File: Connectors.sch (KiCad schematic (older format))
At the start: 11 parts, among them J201 Conn_01x10, J202 Conn_ARM_JTAG_SWD_10, J203 Conn_02x03_Counter_Clockwise, J204 USB_B_Micro, J205 Conn_01x04

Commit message: completed layout
Signed-off-by: Thomas Schmid <tom@binary-kitchen.de>
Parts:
- added U201: USBLC6-2SC6, Package_TO_SOT_SMD:SOT-666, symbol Power_Protection:USBLC6-2SC6
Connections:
- net GND: now also U201.2 (GND)
- net USB_D_N: now also U201.6 (IO1); no longer J204.2 (D-)
- net USB_D_P: now also U201.4 (IO2); no longer J204.3 (D+), R201.1
- net VBUS: now also U201.5 (VBUS)
- new net: J204.2 (D-), U201.1 (IO1)
- new net: J204.3 (D+), R201.1, U201.3 (IO2)
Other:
- moved on the sheet: C202, C203
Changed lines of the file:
@@
 Wire Wire Line
 	3750 1950 3750 1850
-Wire Wire Line
-	4150 1250 4500 1250
 $Comp
 L power:VBUS #PWR0206
@@
 	0    1    1    0
 $EndComp
-Wire Wire Line
-	4650 1450 5100 1450
 Connection ~ 4650 1450
 Wire Wire Line
@@
 Wire Wire Line
 	4150 1450 4650 1450
-Wire Wire Line
-	4150 1550 5100 1550
-Text GLabel 5100 1450 2    50   Input ~ 0
+Text GLabel 6200 950  2    50   Input ~ 0
+USB_D_N
+Text GLabel 6200 2150 2    50   Input ~ 0
 USB_D_P
-Text GLabel 5100 1550 2    50   Input ~ 0
-USB_D_N
 Text GLabel 1400 3050 0    50   Input ~ 0
 PYRO0_HIGH
@@
 L Device:C C202
 U 1 1 5D5800D9
-P 2700 4150
-F 0 "C202" H 2815 4196 50  0000 L CNN
-F 1 "C" H 2815 4105 50  0000 L CNN
-F 2 "Capacitor_SMD:C_0402_1005Metric" H 2738 4000 50  0001 C CNN
-F 3 "~" H 2700 4150 50  0001 C CNN
-	1    2700 4150
+P 1550 4500
+F 0 "C202" H 1665 4546 50  0000 L CNN
+F 1 "C" H 1665 4455 50  0000 L CNN
+F 2 "Capacitor_SMD:C_0402_1005Metric" H 1588 4350 50  0001 C CNN
+F 3 "~" H 1550 4500 50  0001 C CNN
+	1    1550 4500
 	1    0    0    -1
 $EndComp
@@
 L power:+5V #PWR0157
 U 1 1 5D581C2C
-P 2700 4000
-F 0 "#PWR0157" H 2700 3850 50  0001 C CNN
-F 1 "+5V" V 2715 4128 50  0000 L CNN
-F 2 "" H 2700 4000 50  0001 C CNN
-F 3 "" H 2700 4000 50  0001 C CNN
-	1    2700 4000
+P 1550 4350
+F 0 "#PWR0157" H 1550 4200 50  0001 C CNN
+F 1 "+5V" V 1565 4478 50  0000 L CNN
+F 2 "" H 1550 4350 50  0001 C CNN
+F 3 "" H 1550 4350 50  0001 C CNN
+	1    1550 4350
 	1    0    0    -1
 $EndComp
@@
 L power:GND #PWR0158
 U 1 1 5D5820DF
-P 2700 4300
-F 0 "#PWR0158" H 2700 4050 50  0001 C CNN
-F 1 "GND" V 2705 4172 50  0000 R CNN
-F 2 "" H 2700 4300 50  0001 C CNN
-F 3 "" H 2700 4300 50  0001 C CNN
-	1    2700 4300
+P 1550 4650
+F 0 "#PWR0158" H 1550 4400 50  0001 C CNN
+F 1 "GND" V 1555 4522 50  0000 R CNN
+F 2 "" H 1550 4650 50  0001 C CNN
+F 3 "" H 1550 4650 50  0001 C CNN
+	1    1550 4650
 	1    0    0    -1
 $EndComp
@@
 L Device:C C203
 U 1 1 5D584D8C
-P 4200 4100
-F 0 "C203" H 4315 4146 50  0000 L CNN
-F 1 "C" H 4315 4055 50  0000 L CNN
-F 2 "Capacitor_SMD:C_0402_1005Metric" H 4238 3950 50  0001 C CNN
-F 3 "~" H 4200 4100 50  0001 C CNN
-	1    4200 4100
+P 2000 4500
+F 0 "C203" H 2115 4546 50  0000 L CNN
+F 1 "C" H 2115 4455 50  0000 L CNN
+F 2 "Capacitor_SMD:C_0402_1005Metric" H 2038 4350 50  0001 C CNN
+F 3 "~" H 2000 4500 50  0001 C CNN
+	1    2000 4500
 	1    0    0    -1
 $EndComp
@@
 L power:GND #PWR0159
 U 1 1 5D584D98
-P 4200 4250
-F 0 "#PWR0159" H 4200 4000 50  0001 C CNN
-F 1 "GND" V 4205 4122 50  0000 R CNN
-F 2 "" H 4200 4250 50  0001 C CNN
-F 3 "" H 4200 4250 50  0001 C CNN
-	1    4200 4250
+P 2000 4650
+F 0 "#PWR0159" H 2000 4400 50  0001 C CNN
+F 1 "GND" V 2005 4522 50  0000 R CNN
+F 2 "" H 2000 4650 50  0001 C CNN
+F 3 "" H 2000 4650 50  0001 C CNN
+	1    2000 4650
 	1    0    0    -1
 $EndComp
@@
 L power:+3.3V #PWR0160
 U 1 1 5D585061
-P 4200 3950
-F 0 "#PWR0160" H 4200 3800 50  0001 C CNN
-F 1 "+3.3V" H 4215 4123 50  0000 C CNN
-F 2 "" H 4200 3950 50  0001 C CNN
-F 3 "" H 4200 3950 50  0001 C CNN
-	1    4200 3950
-	1    0    0    -1
-$EndComp
+P 2000 4350
+F 0 "#PWR0160" H 2000 4200 50  0001 C CNN
+F 1 "+3.3V" H 2015 4523 50  0000 C CNN
+F 2 "" H 2000 4350 50  0001 C CNN
+F 3 "" H 2000 4350 50  0001 C CNN
+	1    2000 4350
+	1    0    0    -1
+$EndComp
+$Comp
+L power:GND #PWR0108
+U 1 1 5D7E636A
+P 5400 1550
+F 0 "#PWR0108" H 5400 1300 50  0001 C CNN
+F 1 "GND" H 5405 1377 50  0000 C CNN
+F 2 "" H 5400 1550 50  0001 C CNN
+F 3 "" H 5400 1550 50  0001 C CNN
+	1    5400 1550
+	0    1    1    0
+$EndComp
+Wire Wire Line
+	4150 1250 4500 1250
+$Comp
+L power:VBUS #PWR0161
+U 1 1 5D80B200
+P 6400 1550
+F 0 "#PWR0161" H 6400 1400 50  0001 C CNN
+F 1 "VBUS" H 6415 1723 50  0000 C CNN
+F 2 "" H 6400 1550 50  0001 C CNN
+F 3 "" H 6400 1550 50  0001 C CNN
+	1    6400 1550
+	0    1    1    0
+$EndComp
+Wire Wire Line
+	4150 1550 5100 1550
+Wire Wire Line
+	5200 1450 5200 2150
+Wire Wire Line
+	5800 2150 5800 2050
+Wire Wire Line
+	4650 1450 5200 1450
+Wire Wire Line
+	5100 1550 5100 950
+Wire Wire Line
+	5800 950  5800 1050
+$Comp
+L Power_Protection:USBLC6-2SC6 U201
+U 1 1 5D7DF314
+P 5900 1550
+F 0 "U201" V 6050 1900 50  0000 L CNN
+F 1 "USBLC6-2SC6" V 6150 1900 50  0000 L CNN
+F 2 "Package_TO_SOT_SMD:SOT-666" H 5150 1950 50  0001 C CNN
+F 3 "http://www2.st.com/resource/en/datasheet/CD00050750.pdf" H 6100 1900 50  0001 C CNN
+	1    5900 1550
+	0    1    1    0
+$EndComp
+Wire Wire Line
+	6200 2150 6000 2150
+Wire Wire Line
+	6000 2150 6000 2050
+Wire Wire Line
+	6000 1050 6000 950
+Wire Wire Line
+	6200 950  6000 950
+Wire Wire Line
+	5200 2150 5800 2150
+Wire Wire Line
+	5100 950  5800 950
 $EndSCHEMATC

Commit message: minor updates
Signed-off-by: Thomas Schmid <tom@lfence.de>
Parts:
- C201, C202, C203: value C -> 100n; Mouser_Link (none) -> https://www.mouser.de/ProductDetail/Wurth-Elektronik/885012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; Parnumber (none) -> 885012205037
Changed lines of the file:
@@
 P 1050 4500
 F 0 "C201" H 1165 4546 50  0000 L CNN
-F 1 "C" H 1165 4455 50  0000 L CNN
+F 1 "100n" H 1165 4455 50  0000 L CNN
 F 2 "Capacitor_SMD:C_0402_1005Metric" H 1088 4350 50  0001 C CNN
 F 3 "~" H 1050 4500 50  0001 C CNN
+F 4 "https://www.mouser.de/ProductDetail/Wurth-Elektronik/885012205037?qs=sGAEpiMZZMs0AnBnWHyRQEGbLOF2VP1iQ21DRO%252BfKQRXXkG1Pup5LQ%3D%3D" H 1050 4500 50  0001 C CNN "Mouser_Link"
+F 5 "885012205037" H 1050 4500 50  0001 C CNN "Parnumber"
 	1    1050 4500
 	1    0    0    -1
@@
 P 1550 4500
 F 0 "C202" H 1665 4546 50  0000 L CNN
-F 1 "C" H 1665 4455 50  0000 L CNN
+F 1 "100n" H 1665 4455 50  0000 L CNN
 F 2 "Capacitor_SMD:C_0402_1005Metric" H 1588 4350 50  0001 C CNN
 F 3 "~" H 1550 4500 50  0001 C CNN
+F 4 "https://www.mouser.de/ProductDetail/Wurth-Elektronik/885012205037?qs=sGAEpiMZZMs0AnBnWHyRQEGbLOF2VP1iQ21DRO%252BfKQRXXkG1Pup5LQ%3D%3D" H 1550 4500 50  0001 C CNN "Mouser_Link"
+F 5 "885012205037" H 1550 4500 50  0001 C CNN "Parnumber"
 	1    1550 4500
 	1    0    0    -1
@@
 P 2000 4500
 F 0 "C203" H 2115 4546 50  0000 L CNN
-F 1 "C" H 2115 4455 50  0000 L CNN
+F 1 "100n" H 2115 4455 50  0000 L CNN
 F 2 "Capacitor_SMD:C_0402_1005Metric" H 2038 4350 50  0001 C CNN
 F 3 "~" H 2000 4500 50  0001 C CNN
+F 4 "https://www.mouser.de/ProductDetail/Wurth-Elektronik/885012205037?qs=sGAEpiMZZMs0AnBnWHyRQEGbLOF2VP1iQ21DRO%252BfKQRXXkG1Pup5LQ%3D%3D" H 2000 4500 50  0001 C CNN "Mouser_Link"
+F 5 "885012205037" H 2000 4500 50  0001 C CNN "Parnumber"
 	1    2000 4500
 	1    0    0    -1

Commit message: add some missing mouser links and part numbers to the schematic
Signed-off-by: Thomas Schmid <tom@binary-kitchen.de>
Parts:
- U201: Mouser_Link (none) -> https://www.mouser.de/ProductDetail/STMicroelectronics/USBL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; Parnumber (none) -> USBLC6-2SC6
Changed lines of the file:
@@
 F 2 "Package_TO_SOT_SMD:SOT-666" H 5150 1950 50  0001 C CNN
 F 3 "http://www2.st.com/resource/en/datasheet/CD00050750.pdf" H 6100 1900 50  0001 C CNN
+F 4 "https://www.mouser.de/ProductDetail/STMicroelectronics/USBLC6-2SC6?qs=sGAEpiMZZMvxHShE6Whpu%2FcIE2H5IOBdvREMGHqn6h0%3D" H 5900 1550 50  0001 C CNN "Mouser_Link"
+F 5 "USBLC6-2SC6" H 5900 1550 50  0001 C CNN "Parnumber"
 	1    5900 1550
 	0    1    1    0

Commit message: fix wrong connection of quarz
Signed-off-by: Thomas Schmid <tom@binary-kitchen.de>
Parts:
- U201: value USBLC6-2SC6 -> USBLC6-2P6
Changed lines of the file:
@@
 P 5900 1550
 F 0 "U201" V 6050 1900 50  0000 L CNN
-F 1 "USBLC6-2SC6" V 6150 1900 50  0000 L CNN
+F 1 "USBLC6-2P6" V 6150 1900 50  0000 L CNN
 F 2 "Package_TO_SOT_SMD:SOT-666" H 5150 1950 50  0001 C CNN
 F 3 "http://www2.st.com/resource/en/datasheet/CD00050750.pdf" H 6100 1900 50  0001 C CNN

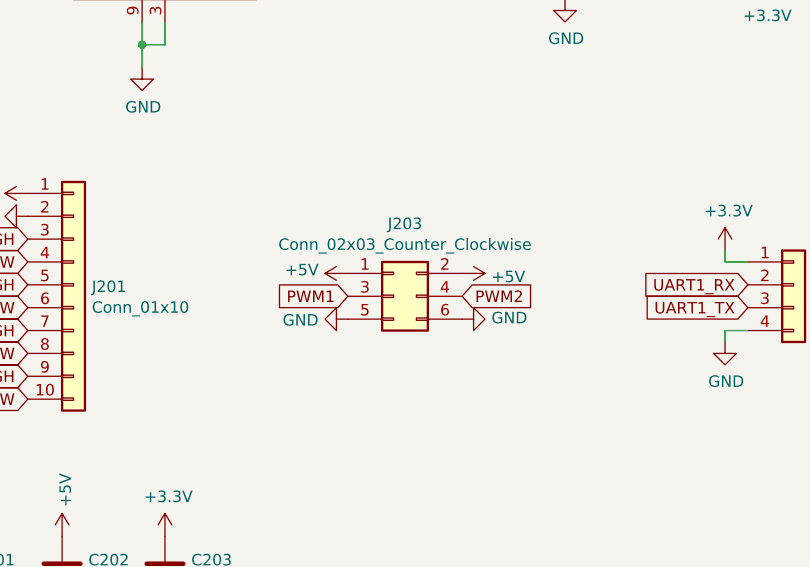
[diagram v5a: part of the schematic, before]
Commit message: fix servo connectors
fix pinout of servo connectors. 5V Pin and Signal was swapped

Signed-off-by: Thomas Schmid <tom@binary-kitchen.de>
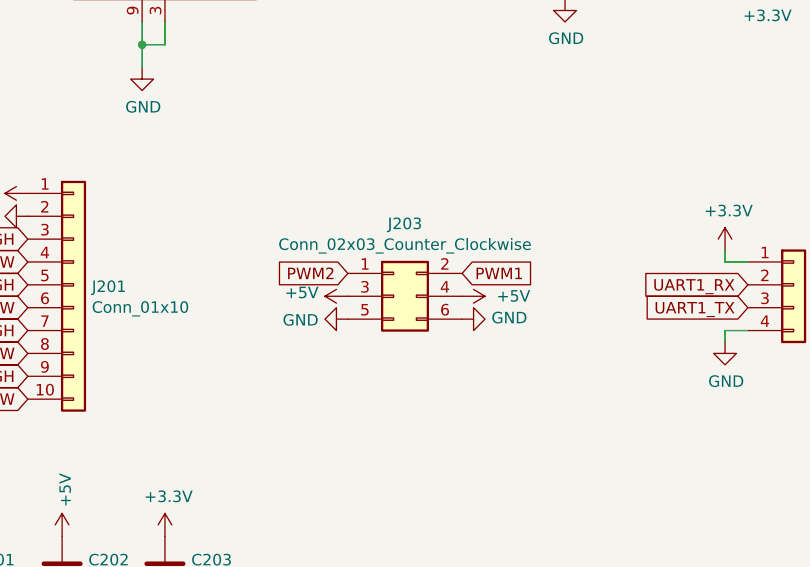
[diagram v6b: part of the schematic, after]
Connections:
- net +5V: now also J203.3 (Pin_3), J203.4 (Pin_4); no longer J203.1 (Pin_1), J203.2 (Pin_2)
- net PWM1: now also J203.2 (Pin_2); no longer J203.3 (Pin_3)
- net PWM2: now also J203.1 (Pin_1); no longer J203.4 (Pin_4)
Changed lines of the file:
@@
 Connection ~ 8350 1250
 NoConn ~ 2500 1700
-Text GLabel 2800 3300 0    50   Input ~ 0
+Text GLabel 3300 3200 2    50   Input ~ 0
 PWM1
-Text GLabel 3300 3300 2    50   Input ~ 0
+Text GLabel 2800 3200 0    50   Input ~ 0
 PWM2
 $Comp
@@
 L power:+5V #PWR0150
 U 1 1 5D546E59
-P 2800 3200
-F 0 "#PWR0150" H 2800 3050 50  0001 C CNN
-F 1 "+5V" V 2815 3328 50  0000 L CNN
-F 2 "" H 2800 3200 50  0001 C CNN
-F 3 "" H 2800 3200 50  0001 C CNN
-	1    2800 3200
+P 2800 3300
+F 0 "#PWR0150" H 2800 3150 50  0001 C CNN
+F 1 "+5V" V 2815 3428 50  0000 L CNN
+F 2 "" H 2800 3300 50  0001 C CNN
+F 3 "" H 2800 3300 50  0001 C CNN
+	1    2800 3300
 	0    -1   -1   0
 $EndComp
@@
 L power:+5V #PWR0151
 U 1 1 5D547AB0
-P 3300 3200
-F 0 "#PWR0151" H 3300 3050 50  0001 C CNN
-F 1 "+5V" V 3315 3328 50  0000 L CNN
-F 2 "" H 3300 3200 50  0001 C CNN
-F 3 "" H 3300 3200 50  0001 C CNN
-	1    3300 3200
+P 3300 3300
+F 0 "#PWR0151" H 3300 3150 50  0001 C CNN
+F 1 "+5V" V 3300 3450 50  0000 L CNN
+F 2 "" H 3300 3300 50  0001 C CNN
+F 3 "" H 3300 3300 50  0001 C CNN
+	1    3300 3300
 	0    1    1    0
 $EndComp

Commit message: v1.2 rev A
Signed-off-by: Thomas Schmid <tom@binary-kitchen.de>
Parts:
- added C204, C205: 100n, Capacitor_SMD:C_0402_1005Metric, symbol Device:C
- added J206: Conn_01x10_MountingPin, Connector_Molex:Molex_PicoBlade_53398-1071_1x10-1MP_P1.25mm_Vertical, symbol Connector_Generic_MountingPin:Conn_01x10_MountingPin
- added R202: 120, Resistor_SMD:R_0603_1608Metric_Pad1.05x0.95mm_HandSolder, symbol Device:R
- added U202: ATA6561, Package_DFN_QFN:DFN-8-1EP_3x3mm_P0.65mm_EP1.55x2.4mm, symbol altimeter:ATA6561
- U201: symbol Power_Protection:USBLC6-2SC6 -> altimeter-rescue:USBLC6-2SC6-Power_Protection
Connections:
- net +3V3: now also C204.1, J206.9 (Pin_9), U202.5 (VIO)
- net +5V: now also C205.1, U202.3 (VCC)
- net GND: now also C204.2, C205.2, J206.10 (Pin_10), J206.MP (MountPin), U202.2 (GND), U202.9 (PAD)
- net USB_D_RAW_N: now reaches J204.2 (D-), U201.1 (IO1)
- net USB_D_RAW_P: now reaches J204.3 (D+), R201.1, U201.3 (IO2)
- new net CAN_H: J206.4 (Pin_4), R202.1, U202.7 (CAN_H)
- new net CAN_L: J206.3 (Pin_3), R202.2, U202.6 (CAN_L)
- new net CAN_RX: U202.4 (RX)
- new net CAN_STDBY: U202.8 (STDBY)
- new net CAN_TX: U202.1 (TX)
- new net GPIO1: J206.7 (Pin_7)
- new net GPIO2: J206.8 (Pin_8)
- new net I2C_SCL: J206.2 (Pin_2)
- new net I2C_SDA: J206.1 (Pin_1)
- new net UART4_RX: J206.6 (Pin_6)
- new net UART4_TX: J206.5 (Pin_5)

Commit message: update
Signed-off-by: Thomas Schmid <tom@binary-kitchen.de>
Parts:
- R202: Mouser_Link https://www.mouser.de/datasheet/2/315/AOA0000C304-1149620.p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 -> https://www.mouser.de/ProductDetail/Panasonic/ERA-3AEB121V?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; Parnumber ERJ-6RBD1200V -> ERA-3AEB121V
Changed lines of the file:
@@
 F 2 "Resistor_SMD:R_0603_1608Metric_Pad1.05x0.95mm_HandSolder" V 6930 3150 50  0001 C CNN
 F 3 "~" H 7000 3150 50  0001 C CNN
-F 4 "https://www.mouser.de/datasheet/2/315/AOA0000C304-1149620.pdf" H 7000 3150 50  0001 C CNN "Mouser_Link"
-F 5 "ERJ-6RBD1200V" H 7000 3150 50  0001 C CNN "Parnumber"
+F 4 "https://www.mouser.de/ProductDetail/Panasonic/ERA-3AEB121V?qs=nho8PGNfA6p7qyQ5b8td6g%3D%3D" H 7000 3150 50  0001 C CNN "Mouser_Link"
+F 5 "ERA-3AEB121V" H 7000 3150 50  0001 C CNN "Parnumber"
 	1    7000 3150
 	1    0    0    -1
